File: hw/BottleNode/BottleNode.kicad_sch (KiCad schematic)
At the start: 16 parts, among them J1 Conn_01x03_Pin, J2 Conn_01x02_Pin

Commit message: schematic and code fragments now agree on pinouts
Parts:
- R1: value DNP -> 0
- R2, R3, R6, R7: value DNP -> DNI
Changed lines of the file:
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@@
       (effects (font (size 1.27 1.27)))
     )
-    (property "Value" "DNP" (at 90.17 132.08 90)
+    (property "Value" "DNI" (at 90.17 132.08 90)
       (effects (font (size 1.27 1.27)))
     )
@@
       (effects (font (size 1.27 1.27)))
     )
-    (property "Value" "DNP" (at 79.375 118.11 90)
+    (property "Value" "DNI" (at 79.375 118.11 90)
       (effects (font (size 1.27 1.27)))
     )
@@
       (effects (font (size 1.27 1.27)))
     )
-    (property "Value" "DNP" (at 189.865 127 90)
+    (property "Value" "DNI" (at 189.865 127 90)
       (effects (font (size 1.27 1.27)))
     )
@@
   (symbol (lib_id "Device:R") (at 79.375 89.535 270) (unit 1)
     (in_bom yes) (on_board yes) (dnp no) (fields_autoplaced)
-    (property "Reference" "R1" (at 79.375 83.185 90)
-      (effects (font (size 1.27 1.27)))
-    )
-    (property "Value" "DNP" (at 79.375 85.725 90)
+    (property "Reference" "R1" (at 79.375 83.82 90)
+      (effects (font (size 1.27 1.27)))
+    )
+    (property "Value" "0" (at 79.375 86.36 90)
       (effects (font (size 1.27 1.27)))
     )
@@
   (symbol (lib_id "Device:R") (at 90.17 89.535 270) (unit 1)
     (in_bom yes) (on_board yes) (dnp no) (fields_autoplaced)
-    (property "Reference" "R2" (at 90.17 83.185 90)
-      (effects (font (size 1.27 1.27)))
-    )
-    (property "Value" "DNP" (at 90.17 85.725 90)
-      (effects (font (size 1.27 1.27)))
-    )
+    (property "Reference" "R2" (at 90.17 83.82 90)
+      (effects (font (size 1.27 1.27)))
+    )
+    (property "Value" "DNI" (at 90.17 86.36 90)
+      (effects (font (size 1.27 1.27)))
+    )

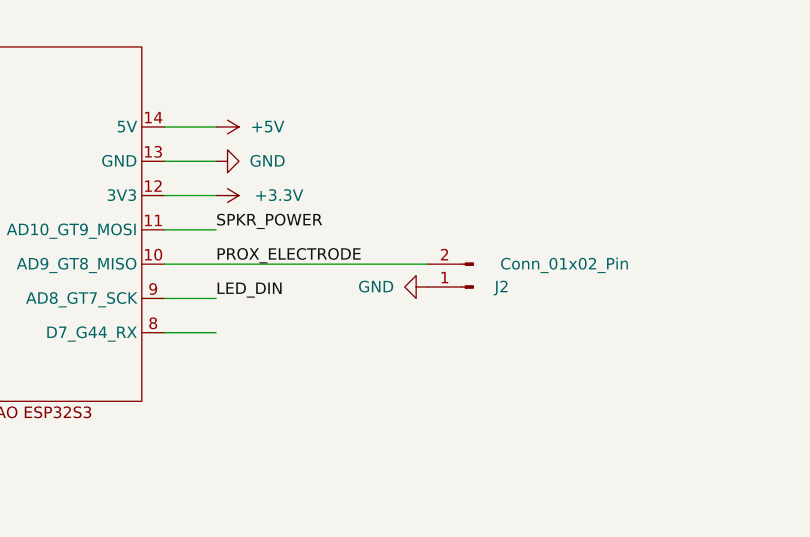
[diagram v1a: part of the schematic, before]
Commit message: swap SPKR_POWER/TOUCH_PIN in AllInOne_test/sch/pcb
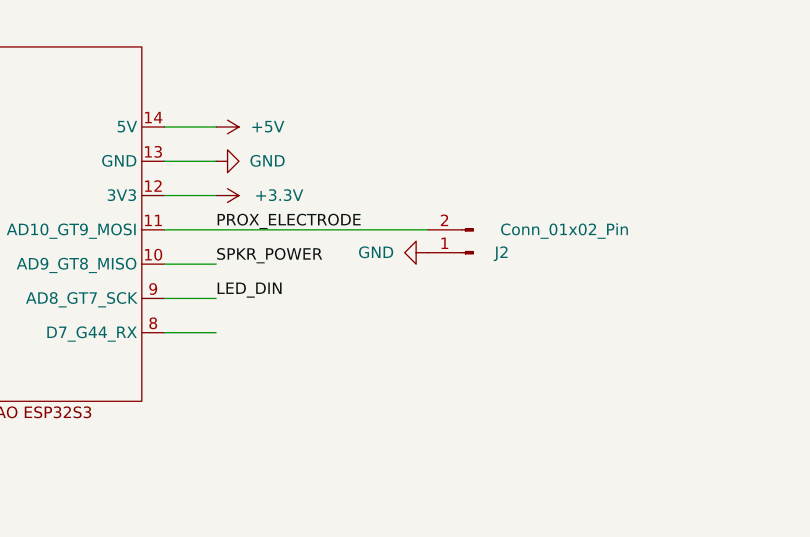
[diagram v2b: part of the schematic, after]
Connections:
- net PROX_ELECTRODE: now also U1.11 (AD10_GT9_MOSI); no longer U1.10 (AD9_GT8_MISO)
- net SPKR_POWER: now also U1.10 (AD9_GT8_MISO); no longer U1.11 (AD10_GT9_MOSI)
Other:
- moved on the sheet: J2
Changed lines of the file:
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@@
+    (stroke (width 0) (type default))
+  )
+  (wire (pts (xy 88.265 45.72) (xy 93.98 45.72))
     (stroke (width 0) (type default))
   )
@@
     (stroke (width 0) (type default))
   )
-  (wire (pts (xy 88.265 41.91) (xy 93.98 41.91))
-    (stroke (width 0) (type default))
-  )
   (wire (pts (xy 72.39 121.92) (xy 75.565 121.92))
     (stroke (width 0) (type default))
   )
-  (wire (pts (xy 88.265 45.72) (xy 117.475 45.72))
+  (wire (pts (xy 88.265 41.91) (xy 117.475 41.91))
     (stroke (width 0) (type default))
   )
@@
     (effects (font (size 1.27 1.27)) (justify right bottom))
   )
-  (label "PROX_ELECTRODE" (at 93.98 45.72 0) (fields_autoplaced)
+  (label "PROX_ELECTRODE" (at 93.98 41.91 0) (fields_autoplaced)
     (effects (font (size 1.27 1.27)) (justify left bottom))
   )
@@
     (effects (font (size 1.27 1.27)) (justify left bottom))
   )
-  (label "SPKR_POWER" (at 93.98 41.91 0) (fields_autoplaced)
+  (label "SPKR_POWER" (at 93.98 45.72 0) (fields_autoplaced)
     (effects (font (size 1.27 1.27)) (justify left bottom))
   )
@@
     )
   )
-  (symbol (lib_id "Connector:Conn_01x02_Pin") (at 122.555 48.26 180) (unit 1)
-    (in_bom yes) (on_board yes) (dnp no)
-    (property "Reference" "J2" (at 125.73 48.26 0)
-      (effects (font (size 1.27 1.27)))
-    )
-    (property "Value" "Conn_01x02_Pin" (at 132.715 45.72 0)
-      (effects (font (size 1.27 1.27)))
-    )
-    (property "Footprint" "Connector_PinHeader_2.54mm:PinHeader_1x02_P2.54mm_Vertical" (at 122.555 48.26 0)
-      (effects (font (size 1.27 1.27)) hide)
-    )
-    (property "Datasheet" "~" (at 122.555 48.26 0)
+  (symbol (lib_id "Connector:Conn_01x02_Pin") (at 122.555 44.45 180) (unit 1)
+    (in_bom yes) (on_board yes) (dnp no)
+    (property "Reference" "J2" (at 125.73 44.45 0)
+      (effects (font (size 1.27 1.27)))
+    )
+    (property "Value" "Conn_01x02_Pin" (at 132.715 41.91 0)
+      (effects (font (size 1.27 1.27)))
+    )
+    (property "Footprint" "Connector_PinHeader_2.54mm:PinHeader_1x02_P2.54mm_Vertical" (at 122.555 44.45 0)
+      (effects (font (size 1.27 1.27)) hide)
+    )
+    (property "Datasheet" "~" (at 122.555 44.45 0)
       (effects (font (size 1.27 1.27)) hide)
     )
@@
     )
   )
-  (symbol (lib_id "power:GND") (at 117.475 48.26 270) (unit 1)
-    (in_bom yes) (on_board yes) (dnp no)
-    (property "Reference" "#PWR013" (at 111.125 48.26 0)
-      (effects (font (size 1.27 1.27)) hide)
-    )
-    (property "Value" "GND" (at 111.76 48.26 90)
-      (effects (font (size 1.27 1.27)))
-    )
-    (property "Footprint" "" (at 117.475 48.26 0)
-      (effects (font (size 1.27 1.27)) hide)
-    )
-    (property "Datasheet" "" (at 117.475 48.26 0)
-      (effects (font (size 1.27 1.27)) hide)
-    )
+  (symbol (lib_id "power:GND") (at 117.475 44.45 270) (unit 1)
+    (in_bom yes) (on_board yes) (dnp no)
+    (property "Reference" "#PWR013" (at 111.125 44.45 0)
+      (effects (font (size 1.27 1.27)) hide)
+    )
+    (property "Value" "GND" (at 111.76 44.45 90)
+      (effects (font (size 1.27 1.27)))
+    )
+    (property "Footprint" "" (at 117.475 44.45 0)
+      (effects (font (size 1.27 1.27)) hide)
+    )
+    (property "Datasheet" "" (at 117.475 44.45 0)
+      (effects (font (size 1.27 1.27)) hide)
+    )

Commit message: rev 1.1 of schematic and PCB layout with BOM
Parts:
- added C1, C2, C3, C4: 10nF, BottleNode:C_0603_1608Metric_Pad1.08x0.95mm_HandSolder, symbol BottleNode:C
- added C5: 1uF, BottleNode:C_0603_1608Metric_Pad1.08x0.95mm_HandSolder, symbol BottleNode:C
- added J3: Conn_01x02_Pin, BottleNode:PinHeader_1x02_P2.54mm_Vertical, symbol BottleNode:Conn_01x02_Pin
- added R8: 100k, BottleNode:R_0603_1608Metric_Pad0.98x0.95mm_HandSolder, symbol BottleNode:R
- D1, D2, D3, D4: footprint LED_SMD:LED_WS2812B_PLCC4_5.0x5.0mm_P3.2mm -> BottleNode:LED_WS2812B_PLCC4_5.0x5.0mm_P3.2mm; symbol LED:WS2812B -> BottleNode:WS2812B
- J1: footprint Connector_PinHeader_2.54mm:PinHeader_1x03_P2.54mm_Vertical -> BottleNode:PinHeader_1x03_P2.54mm_Vertical; symbol Connector:Conn_01x03_Pin -> BottleNode:Conn_01x03_Pin
- J2: footprint Connector_PinHeader_2.54mm:PinHeader_1x02_P2.54mm_Vertical -> BottleNode:PinHeader_1x02_P2.54mm_Vertical; symbol Connector:Conn_01x02_Pin -> BottleNode:Conn_01x02_Pin
- R1, R2, R3, R4, R5, R6, R7: footprint Resistor_SMD:R_0603_1608Metric_Pad0.98x0.95mm_HandSolder -> BottleNode:R_0603_1608Metric_Pad0.98x0.95mm_HandSolder; symbol Device:R -> BottleNode:R
- U1: footprint Seeed Studio XIAO Series Library:XIAO-Generic-Hybrid-14P-2.54-21X17.8MM -> BottleNode:XIAO-Generic-Thruhole-14P-2.54-21X17.8MM; symbol BottleNode_symbols:Seeed_Studio_XIAO_ESP32S3 -> BottleNode:Seeed_Studio_XIAO_ESP32S3
- U2: footprint BottleNode_footprints:INMP441_breakout -> BottleNode:INMP441_breakout; symbol BottleNode_symbols:INMP441_breakout -> BottleNode:INMP441_breakout
- U3: footprint BottleNode_footprints:MAX98357A_adafruit_breakout -> BottleNode:MAX98357A_adafruit_breakout; symbol BottleNode_symbols:MAX98357A_adafruit_breakout -> BottleNode:MAX98357A_adafruit_breakout
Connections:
- net +3.3V: now also C1.1, C2.1, C3.1, C4.1
- net +5V: now also J3.2 (Pin_2)
- net GND: now also C1.2, C2.2, C3.2, C4.2, C5.1, J3.1 (Pin_1), R8.1
- net MIC_SD: now also R8.2
- net SPKR_POWER: now also C5.2
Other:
- moved on the sheet: D4

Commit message: final tweaks on PCB v1.1
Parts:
- U1: value ~ -> XIAO ESP32S3
- U2: value ~ -> INMP441 breakout
- U3: value ~ -> MAX98357A breakout
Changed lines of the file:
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@@
       (effects (font (size 1.27 1.27)) (justify left))
     )
-    (property "Value" "~" (at 36.83 106.68 0)
+    (property "Value" "INMP441 breakout" (at 36.83 106.68 0)
       (effects (font (size 1.27 1.27)))
     )
@@
       (effects (font (size 1.27 1.27)) (justify left))
     )
-    (property "Value" "~" (at 39.37 137.16 0)
+    (property "Value" "MAX98357A breakout" (at 39.37 137.16 0)
       (effects (font (size 1.27 1.27)))
     )
@@
       (effects (font (size 1.27 1.27)))
     )
-    (property "Value" "~" (at 66.675 40.64 0)
-      (effects (font (size 1.27 1.27)))
-    )
+    (property "Value" "XIAO ESP32S3" (at 66.675 40.64 0)
+      (effects (font (size 1.27 1.27)))
+    )
